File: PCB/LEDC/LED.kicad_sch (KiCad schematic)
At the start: 34 parts, among them J1 Reset, J2 Wago, J3 TC2030-USB-NL-DS, J5 USB-C-Socket-H, SW1 Button, U1 ICS43434_MEMS_Mic, U2 ESP32-S3-MINI-1, U5 MD8942

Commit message: Tidy SS
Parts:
- SW1: now not fitted
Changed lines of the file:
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@@
 		(in_bom no)
 		(on_board yes)
-		(dnp no)
+		(dnp yes)
 		(fields_autoplaced yes)
 		(property "Reference" "SW1"

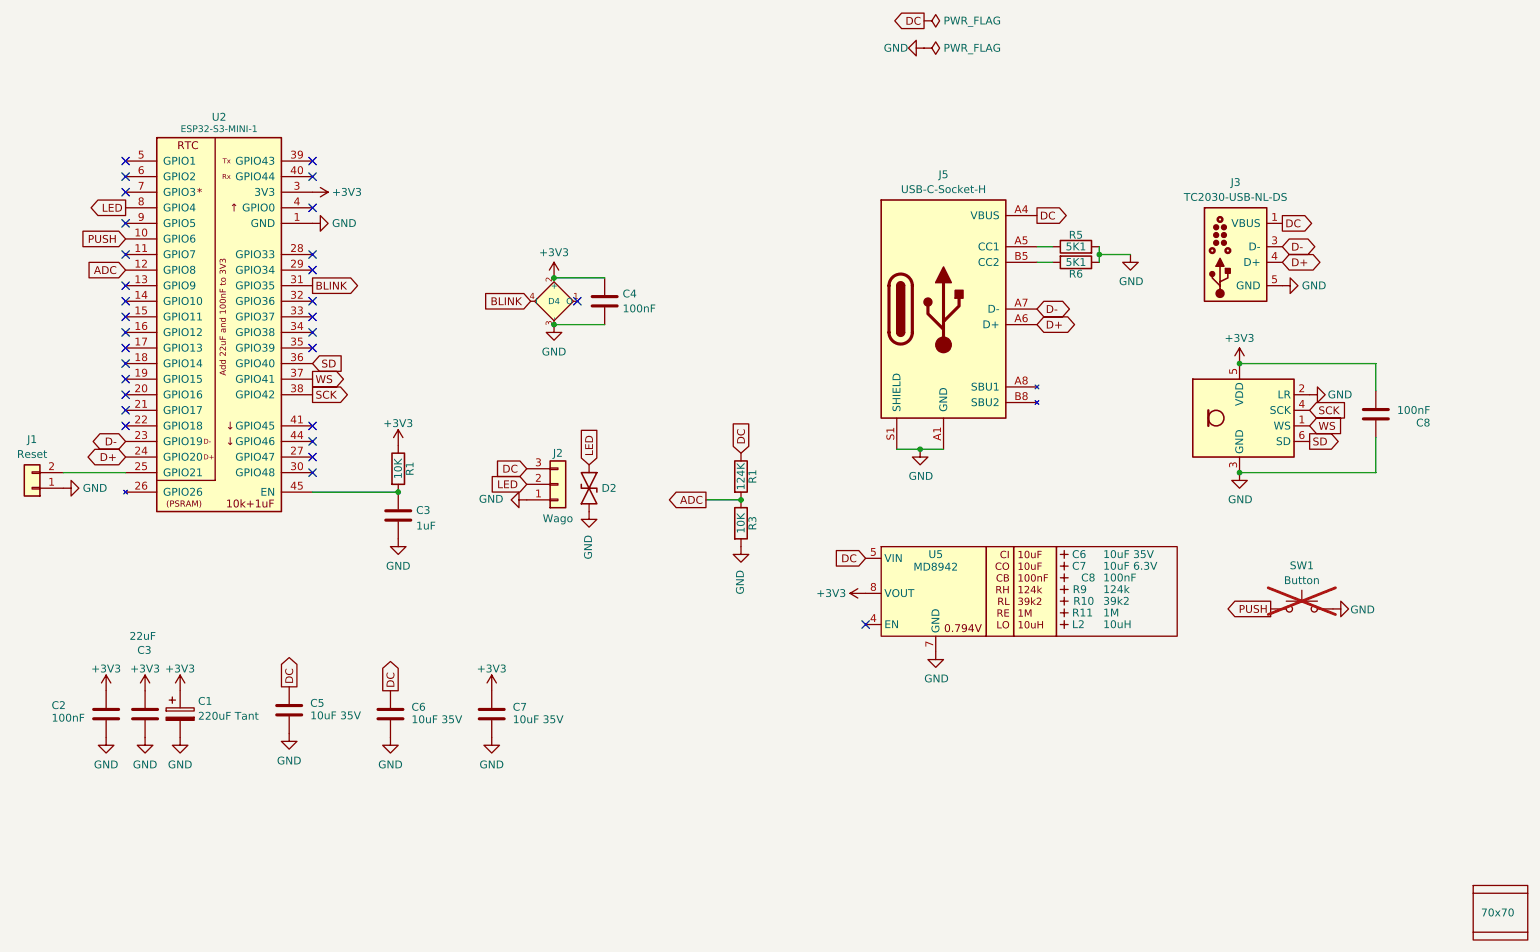
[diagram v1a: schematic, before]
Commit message: Reworked layout
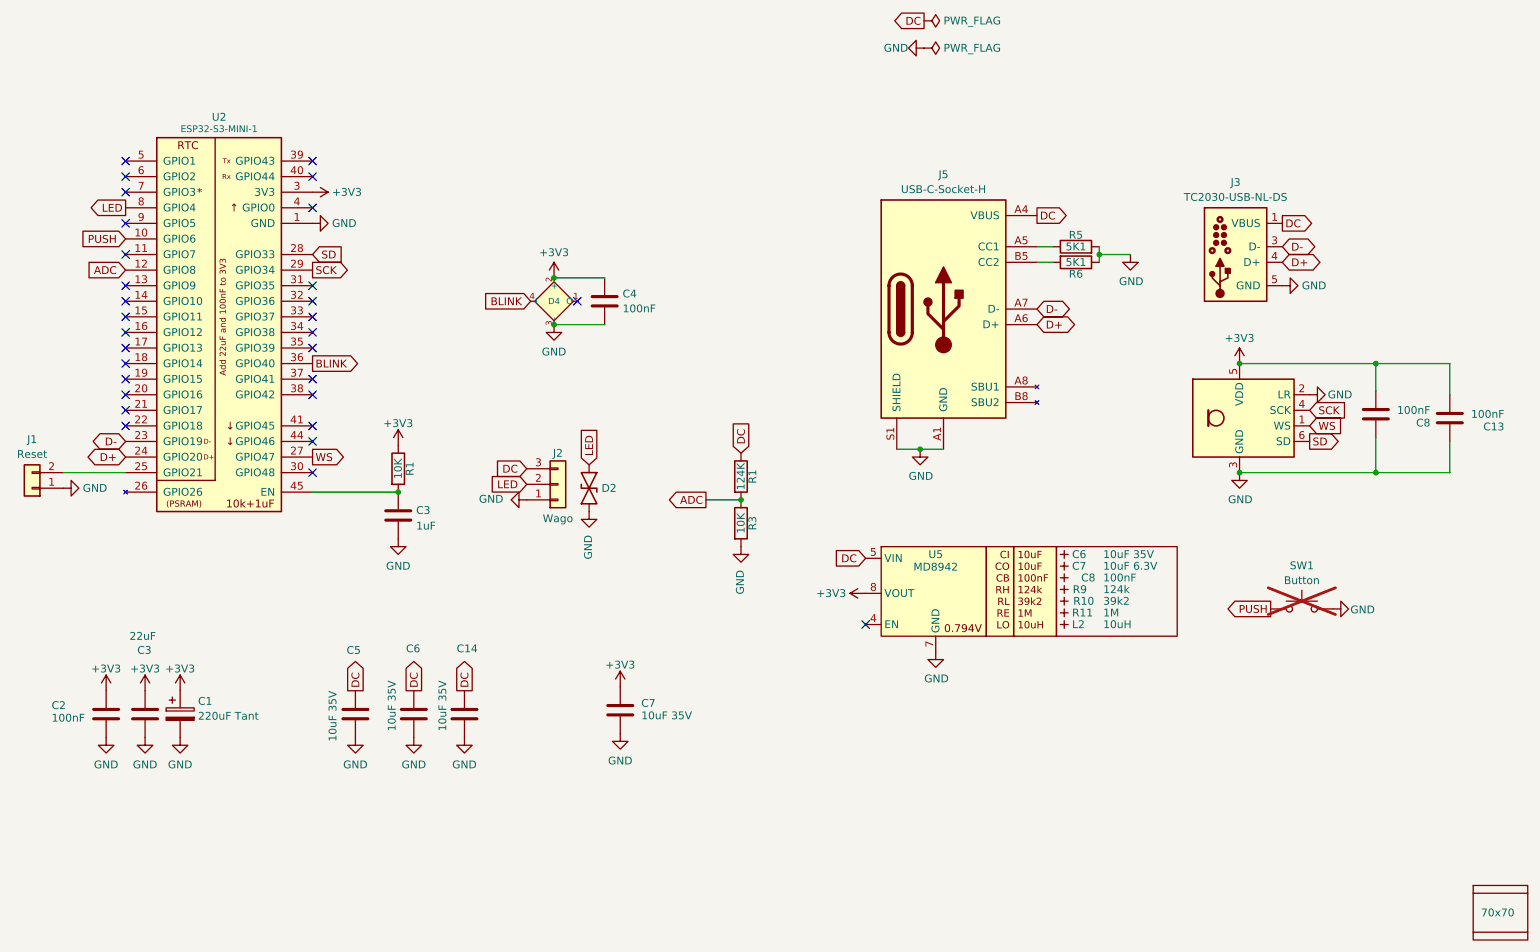
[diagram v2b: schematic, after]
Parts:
- added C13: 100nF, RevK:C_0402, symbol Device:C
- added C14: 10uF 35V, RevK:C_0603, symbol Device:C
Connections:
- net +3V3: now also C13.2
- net BLINK: now also U2.36 (GPIO40); no longer U2.31 (GPIO35)
- net DC: now also C5.2, C14.1; no longer C5.1
- net GND: now also C5.1, C13.1, C14.2; no longer C5.2
- net SCK: now also U2.29 (GPIO34); no longer U2.38 (GPIO42)
- net SD: now also U2.28 (GPIO33); no longer U2.36 (GPIO40)
- net WS: now also U2.27 (GPIO47); no longer U2.37 (GPIO41)
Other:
- moved on the sheet: C5, C6, C7

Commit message: tidy
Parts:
- renumbered C6 to C10, C7 to C11, C8 to C12, C3 to C9, D4 to D1, R10 to R14, R11 to R15, R1 to R2, R9 to R4, U2 to U6, U5 to U7
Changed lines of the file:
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@@
 (kicad_sch
-	(version 20231120)
+	(version 20241209)
 	(generator "eeschema")
-	(generator_version "8.0")
+	(generator_version "9.0")
 	(paper "A4")
 	(title_block
@@
 		(on_board yes)
 		(dnp no)
-		(property "Reference" "C6"
+		(property "Reference" "C10"
 			(at 189.865 114.935 0)
 			(effects
@@
 		(on_board yes)
 		(dnp no)
-		(property "Reference" "C8"
+		(property "Reference" "C12"
 			(at 193.675 118.745 90)
 			(effects
@@
 		(on_board yes)
 		(dnp no)
-		(property "Reference" "R11"
+		(property "Reference" "R15"
 			(at 189.865 124.46 0)
 			(effects
@@
 		(dnp no)
 		(fields_autoplaced yes)
-		(property "Reference" "#PWR0105"
+		(property "Reference" "#PWR022"
 			(at 80.01 118.745 0)
 			(effects
@@
 		(on_board yes)
 		(dnp no)
-		(property "Reference" "R9"
+		(property "Reference" "R4"
 			(at 191.135 120.65 0)
 			(effects
@@
 		(dnp no)
 		(fields_autoplaced yes)
-		(property "Reference" "U2"
+		(property "Reference" "U6"
 			(at 50.8 43.6332 0)
 			(effects
@@
 		(dnp no)
 		(fields_autoplaced yes)
-		(property "Reference" "#PWR03"
+		(property "Reference" "#PWR019"
 			(at 62.23 55.88 0)
 			(effects
@@
 		(on_board yes)
 		(dnp no)
-		(property "Reference" "#PWR010"
+		(property "Reference" "#PWR025"
 			(at 167.64 137.16 0)
 			(effects
@@
 		(dnp no)
 		(fields_autoplaced yes)
-		(property "Reference" "#PWR0106"
+		(property "Reference" "#PWR021"
 			(at 80.01 100.965 0)
 			(effects
@@
 		(dnp no)
 		(fields_autoplaced yes)
-		(property "Reference" "#PWR01"
+		(property "Reference" "#PWR020"
 			(at 72.39 60.96 0)
 			(effects
@@
 		(on_board yes)
 		(dnp no)
-		(property "Reference" "D4"
+		(property "Reference" "D1"
 			(at 105.41 73.66 0)
 			(do_not_autoplace yes)
@@
 		(on_board yes)
 		(dnp no)
-		(property "Reference" "R1"
+		(property "Reference" "R2"
 			(at 81.915 100.965 90)
 			(effects
@@
 		(dnp no)
 		(fields_autoplaced yes)
-		(property "Reference" "#PWR019"
+		(property "Reference" "#PWR09"
 			(at 105.41 83.82 0)
 			(effects
@@
 		(on_board yes)
 		(dnp no)
-		(property "Reference" "U5"
+		(property "Reference" "U7"
 			(at 167.64 114.935 0)
 			(effects
@@
 		(on_board yes)
 		(dnp no)
-		(property "Reference" "C7"
+		(property "Reference" "C11"
 			(at 189.865 116.84 0)
 			(effects
@@
 		(dnp no)
 		(fields_autoplaced yes)
-		(property "Reference" "#PWR09"
+		(property "Reference" "#PWR024"
 			(at 160.02 121.285 0)
 			(effects
@@
 		(dnp no)
 		(fields_autoplaced yes)
-		(property "Reference" "C3"
+		(property "Reference" "C9"
 			(at 82.931 107.7503 0)
 			(effects
@@
 		(on_board yes)
 		(dnp no)
-		(property "Reference" "R10"
+		(property "Reference" "R14"
 			(at 191.77 122.555 90)
 			(effects
@@
 		)
 	)
+	(embedded_fonts no)
 )

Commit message: PCB Update
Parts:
- C1: JLCPCB Rotation Offset 180 -> (none); LCSC Part # C122649 -> (none); MPN (none) -> C122649
- C10, C14, C5, C6, C7: LCSC Part # C194427 -> (none); MPN (none) -> C194427
- C11: LCSC Part # C1691 -> (none); MPN (none) -> C1691
- D1: LCSC Part # C5349953 -> (none); MPN (none) -> C5349953
- D2: LCSC Part # C5137770 -> (none); MPN (none) -> C5137770
- J2: LCSC Part # C2765056 -> (none); MPN (none) -> C2765056
- J5: LCSC Part # C709357 -> (none); MPN (none) -> C709357
- U1: LCSC Part # C5656610 -> (none); MPN (none) -> C5656610
- U6: LCSC Part # C3013941 -> (none); MPN (none) -> C3013941
- U7: LCSC Part # C2684786 -> (none); MPN (none) -> C2684786
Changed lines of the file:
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@@
 			)
 		)
-		(property "LCSC Part #" "C194427"
+		(property "MPN" "C194427"
 			(at 188.595 114.935 0)
 			(effects
@@
 			)
 		)
-		(property "LCSC Part #" "C194427"
+		(property "MPN" "C194427"
 			(at 116.205 140.335 0)
 			(effects
@@
 			)
 		)
-		(property "LCSC Part #" "C2765056"
+		(property "MPN" "C2765056"
 			(at 106.045 103.505 0)
 			(effects
@@
 			)
 		)
-		(property "LCSC Part #" "C5137770"
+		(property "MPN" "C5137770"
 			(at 107.95 104.14 0)
 			(effects
@@
 			)
 		)
-		(property "LCSC Part #" "C3013941"
+		(property "MPN" "C3013941"
 			(at 50.8 109.855 0)
 			(effects
@@
 			)
 		)
-		(property "LCSC Part #" "C194427"
+		(property "MPN" "C194427"
 			(at 73.025 140.97 0)
 			(effects
@@
 			)
 		)
-		(property "LCSC Part #" "C194427"
+		(property "MPN" "C194427"
 			(at 90.805 140.97 0)
 			(effects
@@
 			)
 		)
-		(property "LCSC Part #" "C709357"
+		(property "MPN" "C709357"
 			(at 168.91 74.93 0)
 			(effects
@@
 			)
 		)
-		(property "LCSC Part #" "C122649"
-			(at 44.45 140.97 0)
-			(effects
-				(font
-					(size 1.27 1.27)
-				)
-				(hide yes)
-			)
-		)
-		(property "JLCPCB Rotation Offset" "180"
+		(property "MPN" "C122649"
 			(at 44.45 140.97 0)
 			(effects
@@
 			)
 		)
-		(property "LCSC Part #" "C5656610"
+		(property "MPN" "C5656610"
 			(at 223.52 100.838 0)
 			(effects
@@
 			)
 		)
-		(property "LCSC Part #" "C5349953"
+		(property "MPN" "C5349953"
 			(at 106.68 62.23 0)
 			(effects
@@
 			)
 		)
-		(property "LCSC Part #" "C2684786"
+		(property "MPN" "C2684786"
 			(at 167.64 147.955 0)
 			(effects
@@
 			)
 		)
-		(property "LCSC Part #" "C1691"
+		(property "MPN" "C1691"
 			(at 188.595 116.84 0)
 			(effects
@@
 			)
 		)
-		(property "LCSC Part #" "C194427"
+		(property "MPN" "C194427"
 			(at 82.55 140.97 0)
 			(effects

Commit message: New README
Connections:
- net D-: now also J3.2 (NC), J3.6 (NC)
- net DC: no longer J3.2 (VBUS)
- net GND: no longer J3.6 (GND)
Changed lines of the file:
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@@
 			)
 		)
-		(property "Datasheet" " ~"
+		(property "Datasheet" "~"
 			(at 220.345 67.31 0)
 			(effects

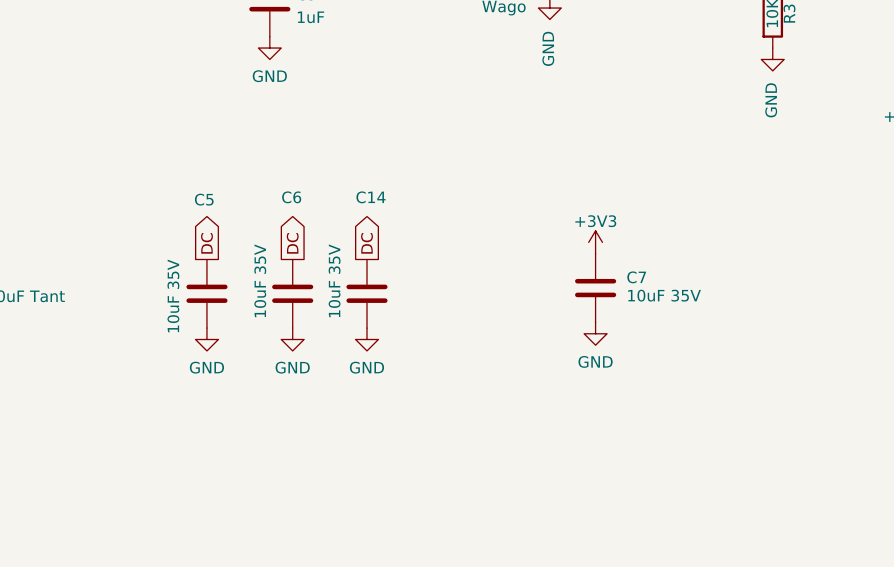
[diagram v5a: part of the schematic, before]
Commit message: Larger caps
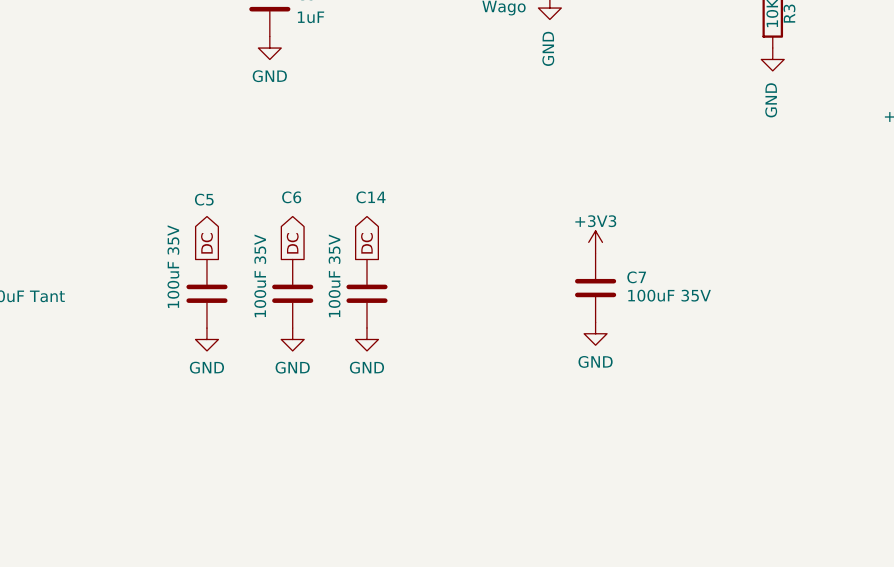
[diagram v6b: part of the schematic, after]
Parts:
- C14, C5, C6, C7: value 10uF 35V -> 100uF 35V; MPN C194427 -> C385964
- L2: MPN (none) -> C167879
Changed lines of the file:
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@@
 (kicad_sch
-	(version 20241209)
+	(version 20250114)
 	(generator "eeschema")
 	(generator_version "9.0")
@@
 			)
 		)
-		(property "Value" "10uF 35V"
+		(property "Value" "100uF 35V"
 			(at 119.634 141.224 0)
 			(effects
@@
 			)
 		)
-		(property "MPN" "C194427"
+		(property "MPN" "C385964"
 			(at 116.205 140.335 0)
 			(effects
@@
 			)
 		)
-		(property "Value" "10uF 35V"
-			(at 69.342 137.16 90)
+		(property "Value" "100uF 35V"
+			(at 69.342 133.35 90)
 			(effects
 				(font
@@
 			)
 		)
-		(property "MPN" "C194427"
+		(property "MPN" "C385964"
 			(at 73.025 140.97 0)
 			(effects
@@
 			)
 		)
-		(property "Value" "10uF 35V"
+		(property "Value" "100uF 35V"
 			(at 87.249 143.764 90)
 			(effects
@@
 			)
 		)
-		(property "MPN" "C194427"
+		(property "MPN" "C385964"
 			(at 90.805 140.97 0)
 			(effects
@@
 			)
 		)
-		(property "Part No" ""
-			(at 188.595 126.365 0)
-			(effects
-				(font
-					(size 1.27 1.27)
-				)
-				(hide yes)
-			)
-		)
-		(property "Note" ""
-			(at 188.595 126.365 0)
+		(property "MPN" "C167879"
+			(at 188.595 126.365 90)
 			(effects
 				(font
@@
 			)
 		)
-		(property "Value" "10uF 35V"
+		(property "Value" "100uF 35V"
 			(at 78.994 143.764 90)
 			(effects
@@
 			)
 		)
-		(property "MPN" "C194427"
+		(property "MPN" "C385964"
 			(at 82.55 140.97 0)
 			(effects

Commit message: Bigger caps
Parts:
- removed C14: 100uF 35V, RevK:C_0603, symbol Device:C
- C5, C6, C7: value 100uF 35V -> 22uF 35V; footprint RevK:C_0603 -> RevK:C_0805; MPN C385964 -> C6119901
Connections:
- net DC: now also C5.1; no longer C5.2
- net GND: now also C5.2; no longer C5.1
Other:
- moved on the sheet: C6

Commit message: New design
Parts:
- added C14: 47uF, RevK:C_0603, symbol Device:C
- added R7: 47R, RevK:R_0402, symbol Device:R
- added U2: IRMHF384, RevK:IR-SMD-4P,3.35x3.9mm, symbol RevK:IRMHF384
- C1: value 220uF Tant -> 220uF; footprint RevK:CP_EIA-3528-21_Kemet-B -> RevK:C_1206; symbol Device:C_Polarized -> Device:C; MPN C122649 -> C412252
- R1, R4: MPN (none) -> C2933070
- R14: MPN (none) -> C137996
- R15: MPN (none) -> C26083
- R2, R3: MPN (none) -> C25744
- R5, R6: MPN (none) -> C25905
- U1: footprint RevK:ICS43434_MEMS_Mic -> RevK:ICS43434_MEMS_Mic_Open
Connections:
- net +3V3: now also R7.2
- net GND: now also C14.2, U2.3 (GND), U2.4 (GND)
- net IR: now reaches U6.32 (GPIO36)
- net IR: now also U2.1 (OUT)
- new net: C14.1, R7.1, U2.2 (VCC)
- no-connect marks 30 -> 29
